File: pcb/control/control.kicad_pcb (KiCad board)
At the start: 2 copper layers, 68 x 76 mm, 63 parts, among them J1 Conn_01x06, J2 Conn_01x05, J4 USB_B_Micro, J5 Conn_01x04, J7 Conn_01x02, J8 Conn_01x02, SW1 PEC12R-4217F-S0024, U1 E73-2G4M08S1C-52840, U10 DCX114YU, U2 MAX98357A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

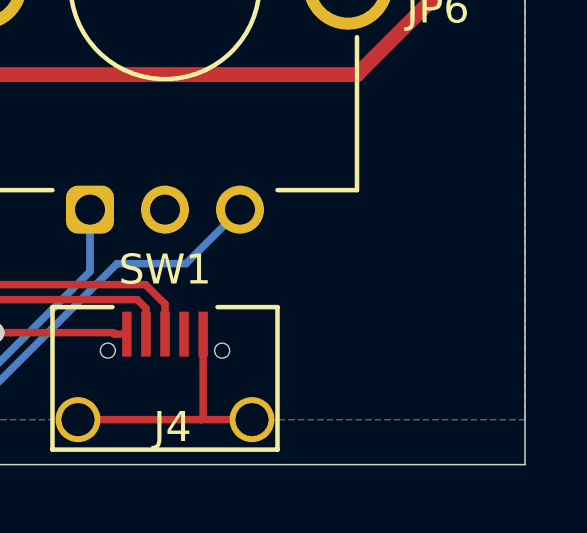
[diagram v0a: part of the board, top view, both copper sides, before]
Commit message: New directory structure and nrf52 os layer
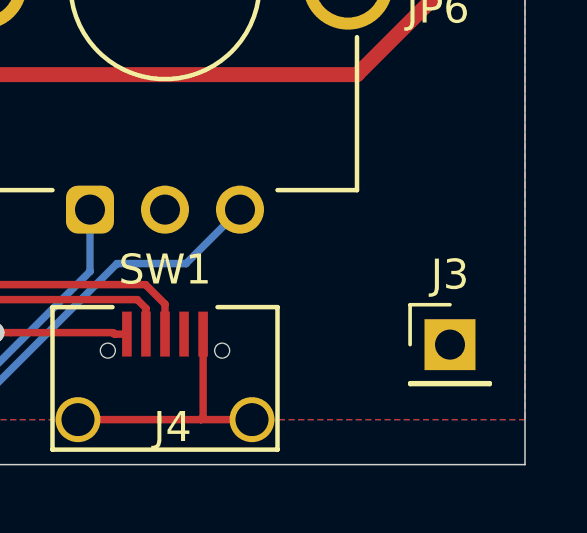
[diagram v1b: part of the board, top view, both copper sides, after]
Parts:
- added J3: Conn_01x01, Connector_PinHeader_2.54mm:PinHeader_1x01_P2.54mm_Vertical, F.Cu at (131.5, 134.0)
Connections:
- net SP_BCLK renamed AU_BCLK
- net SP_DIN renamed AU_DIN
- net SP_EN renamed AU_EN
- net SP_LRCLK renamed AU_LRCLK
- net SWITCH renamed BUTTON

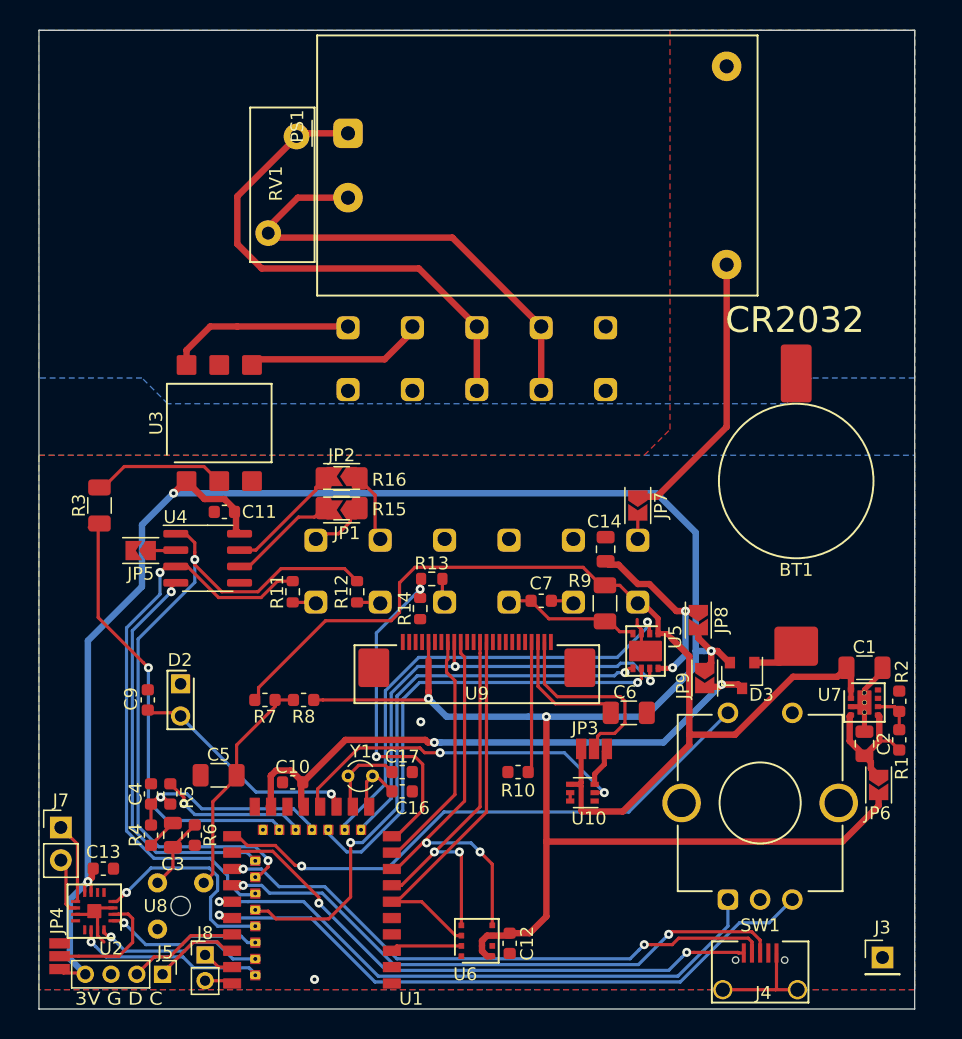
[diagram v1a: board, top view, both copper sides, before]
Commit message: First prototype of PCB and switch to KiCad 6 (#25)
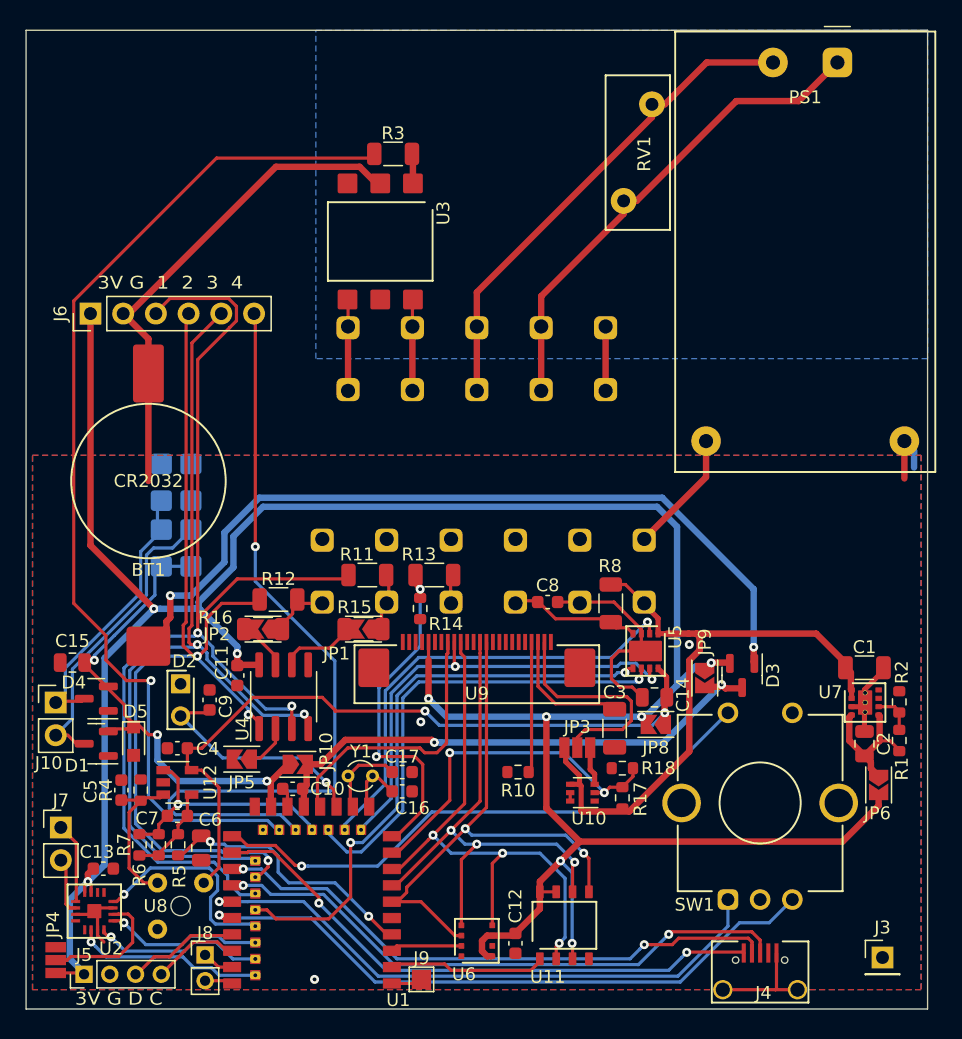
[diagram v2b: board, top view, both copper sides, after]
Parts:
- removed JP7: SolderJumper_2_Open, RoomControl:Jumper2
- removed the R8 at (86.5, 114.0)
- added C15: 22u/6V3, Capacitor_SMD:C_0805_2012Metric, F.Cu at (68.6, 111.1)
- added C7: 10n, Capacitor_SMD:C_0603_1608Metric, F.Cu at (76.8, 123.0)
- added D1: BAS40-04, Package_TO_SOT_SMD:SOT-23, F.Cu at (70.5, 117.4)
- added D4: BAS40-04, Package_TO_SOT_SMD:SOT-23, F.Cu at (70.5, 113.9)
- added D5: D_Zener_Small, Diode_SMD:D_SOD-323F, F.Cu at (73.3, 117.2)
- added D6: D_Small, Diode_SMD:D_1206_3216Metric_Castellated, B.Cu at (77.8, 102.2)
- added D7: D_Small, Diode_SMD:D_1206_3216Metric_Castellated, B.Cu at (75.5, 102.2)
- added D8: D_Small, Diode_SMD:D_1206_3216Metric_Castellated, B.Cu at (77.8, 97.1)
- added D9: D_Small, Diode_SMD:D_1206_3216Metric_Castellated, B.Cu at (75.5, 97.1)
- added J10: Conn_01x02, Connector_PinHeader_2.54mm:PinHeader_1x02_P2.54mm_Vertical, F.Cu at (67.3, 114.2)
- added J6: Conn_01x06, Connector_PinHeader_2.54mm:PinHeader_1x06_P2.54mm_Vertical, F.Cu at (70.0, 84.0)
- added J9: Conn_01x01, TestPoint:TestPoint_Pad_1.5x1.5mm, F.Cu at (95.7, 135.7)
- added JP10: SolderJumper_2_Open, RoomControl:Jumper2, F.Cu at (86.1, 119.0)
- added R17: 47k, Resistor_SMD:R_0603_1608Metric, F.Cu at (111.3, 121.6)
- added R18: 10k, Resistor_SMD:R_0603_1608Metric, F.Cu at (111.3, 119.3)
- added U11: FM25CL64B, RoomControl:FM25CL64B, F.Cu at (106.8, 131.5)
- added U12: MCP6001-OT, Package_TO_SOT_SMD:SOT-23-5, F.Cu at (76.8, 120.4)
- C1: value 10u/25V/X7R -> 10u/16V
- C14, C2: value 22u/16V -> 22u/6V3
- C3: value 22u/16V -> 10u/16V; footprint Capacitor_SMD:C_0805_2012Metric -> Capacitor_SMD:C_1206_3216Metric
- C5: value 10u/25V/X7R -> 10n; footprint Capacitor_SMD:C_1206_3216Metric -> Capacitor_SMD:C_0603_1608Metric
- C6: value 10u/25V/X7R -> 22u/6V3; footprint Capacitor_SMD:C_1206_3216Metric -> Capacitor_SMD:C_0805_2012Metric
- R11, R12, R13: footprint Resistor_SMD:R_0603_1608Metric -> Resistor_SMD:R_1206_3216Metric
- R4: value 10k -> 33k
- R5: value 10M -> 33k
- R6, R7: value 33k -> 10M
- moved BT1 50.3 mm to (74.5, 97.0)
- moved PS1 38.4 mm to (128.0, 64.5), turned to -90 degrees
- moved R3 35.6 mm to (93.5, 71.6), turned to 0 degrees
- moved C3 35.3 mm to (110.7, 116.2)
- moved C6 34.8 mm to (78.6, 125.5), turned to 90 degrees
- moved RV1 27.7 mm to (112.5, 71.5), turned to 90 degrees
- moved U3 18.8 mm to (92.5, 78.4), turned to -90 degrees
- moved JP5 18.0 mm to (81.8, 118.6)
- moved R7 14.9 mm to (73.8, 125.2), turned to 90 degrees
- moved JP2 13.3 mm to (83.4, 108.5)
- moved R16 13.2 mm to (83.4, 108.5)
- moved C11 12.7 mm to (81.4, 112.1), turned to 90 degrees
- moved U4 12.3 mm to (85.0, 113.8), turned to 90 degrees
- moved C14 12.1 mm to (113.8, 113.8), turned to 0 degrees
- moved R15 9.55 mm to (91.2, 108.5)
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- renumbered C7 to C8, R9 to R8
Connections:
- C14 pad 2: Net-(C14-Pad2) -> +3.3VA
- C3 pad 2: Net-(C3-Pad2) -> GND
- C4 pad 2: MD_COMP -> +3.3VA
- C5 pad 1: Net-(C5-Pad1) -> GND
- C5 pad 2: GND -> Net-(C5-Pad2)
- C6 pad 1: Net-(C6-Pad1) -> GND
- C6 pad 2: GND -> MD_N
- J1 pad 1: EXT1 -> EXT2
- J1 pad 2: EXT2 -> EXT1
- J4 pad 4: Net-(J4-Pad4) -> unconnected-(J4-Pad4)
- J5 pad 1: SWDCLK -> +3V3
- J5 pad 2: SWDIO -> GND
- J5 pad 3: GND -> SWDIO
- J5 pad 4: +3V3 -> SWDCLK
- JP8 pad 1: Net-(C14-Pad2) -> +3.3VA
- PS1 pad 1: L -> N
- PS1 pad 2: N -> L
- PS1 pad 4: Net-(JP7-Pad1) -> +12V
- R4 pad 1: Net-(C3-Pad1) -> GND
- R4 pad 2: MD_COMP -> Net-(C5-Pad2)
- R5 pad 1: MD_COMP -> MD_N
- R5 pad 2: MD_DS -> Net-(C7-Pad1)
- R6 pad 1: GND -> Net-(C7-Pad1)
- R6 pad 2: Net-(C3-Pad2) -> MD_P
- R7 pad 1: Net-(C5-Pad1) -> Net-(C7-Pad1)
- R7 pad 2: +12V -> MD_P
- RV1 pad 1: L -> N
- RV1 pad 2: N -> L
- U1 pad 17: EN_12V -> DISP_CS
- U1 pad 18: MD_COMP -> MD_P
- U1 pad 2: Net-(U1-Pad2) -> FERAM_CS
- U1 pad 20: MD_DS -> PIN4
- U1 pad 23: Net-(C10-Pad1) -> GENERATOR
- U1 pad 25: Net-(U1-Pad25) -> unconnected-(U1-Pad25)
- U1 pad 4: Net-(U1-Pad4) -> MD_N
- U1 pad 9: DISP_CS -> EN_12V
- U2 pad 12: Net-(U2-Pad12) -> unconnected-(U2-Pad12)
- U2 pad 13: Net-(U2-Pad13) -> unconnected-(U2-Pad13)
- U2 pad 5: Net-(U2-Pad5) -> unconnected-(U2-Pad5)
- U2 pad 6: Net-(U2-Pad6) -> unconnected-(U2-Pad6)
- U3 pad 1: +3V3 -> Net-(R3-Pad2)
- U3 pad 2: Net-(R3-Pad2) -> GND
- U3 pad 3: Net-(U3-Pad3) -> unconnected-(U3-Pad3)
- U3 pad 4: H2 -> H1
- U3 pad 5: Net-(U3-Pad5) -> unconnected-(U3-Pad5)
- U3 pad 6: H1 -> H2
- U5 pad 8: Net-(C14-Pad2) -> +3.3VA
- U7 pad 7: Net-(U7-Pad7) -> unconnected-(U7-Pad7)
- U7 pad 8: Net-(U7-Pad8) -> unconnected-(U7-Pad8)
- U8 pad 1: Net-(C5-Pad1) -> +3.3VA
- U8 pad 2: Net-(C3-Pad2) -> Net-(C5-Pad2)
- U9 pad 15: Net-(U9-Pad15) -> unconnected-(U9-Pad15)
- U9 pad 22: Net-(C6-Pad1) -> Net-(C3-Pad1)
- U9 pad 4: Net-(U9-Pad4) -> unconnected-(U9-Pad4)
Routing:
- net PIN4: track 0.00 -> 63.7 mm, vias 0 -> 1
- net Net-(BT1-Pad1): track 3.78 -> 63.1 mm, vias 0 -> 2
- net GND: track 25.5 -> 83.5 mm, vias 2 -> 3
- net +3.3VA: track 0.00 -> 57.2 mm, vias 0 -> 2
- net H: track 34.7 -> 81.3 mm
- net PIN1: track 45.5 -> 90.6 mm, vias 1 -> 2
- net GENERATOR: track 0.00 -> 38.9 mm, vias 0 -> 3
- net PIN3: track 31.1 -> 68.5 mm, vias 1 -> 2
- net G1: track 0.00 -> 26.4 mm
- net +12V: track 85.2 -> 59.9 mm
- net Net-(JP7-Pad1): track 21.7 -> 0.00 mm
- net G2: track 0.00 -> 21.3 mm
- net MD_N: track 0.00 -> 21.3 mm, vias 0 -> 2
- net PIN2: track 53.9 -> 73.7 mm, vias 2 -> 3
- net MD_P: track 0.00 -> 19.1 mm, vias 0 -> 1
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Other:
- board size 68 x 76 mm -> 70 x 76 mm
- net class Default removed
- net class Mains removed
- board text added: "3V G 1 2 3 4"
